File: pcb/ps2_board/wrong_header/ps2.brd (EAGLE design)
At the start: 56 x 65 mm, 35 parts, among them IC3 STM32F042F4, SW4 324_SW, U1 MAX3232

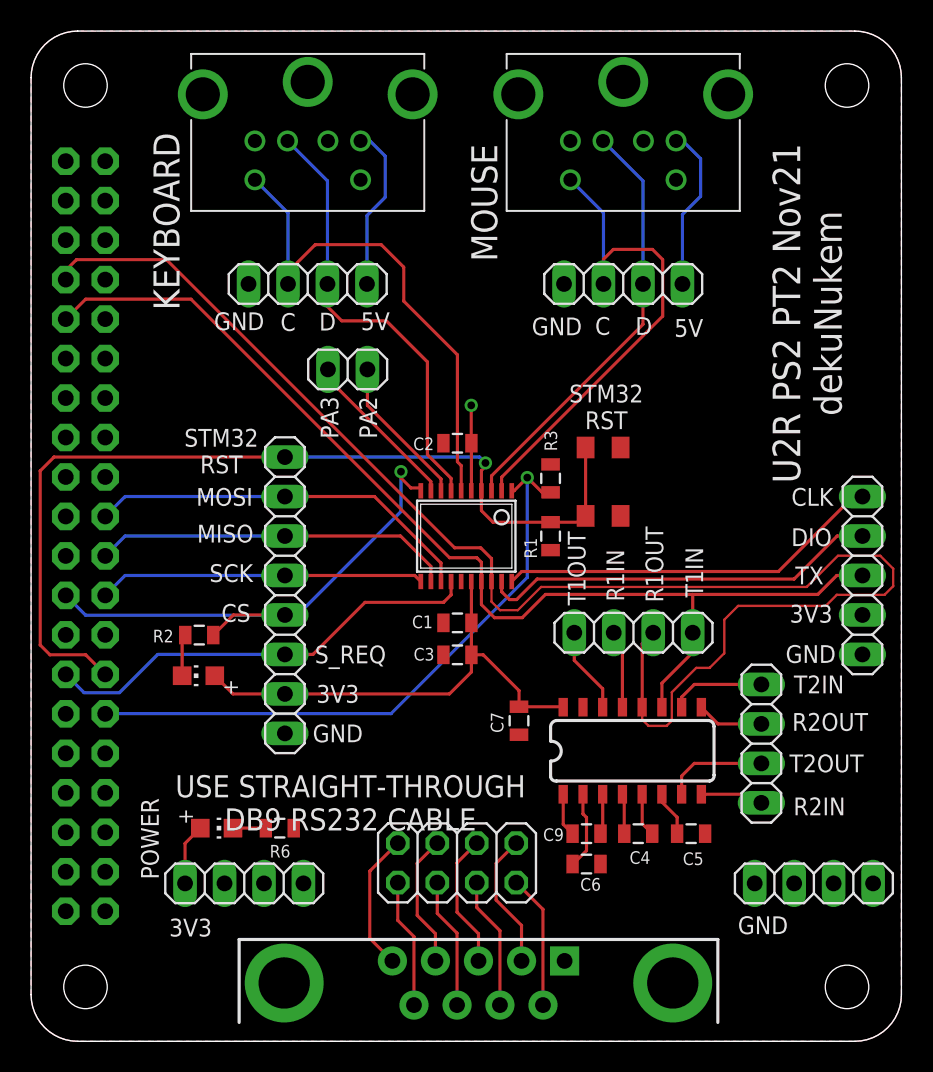
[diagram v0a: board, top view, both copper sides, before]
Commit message: fixed header orientation on ps2 board
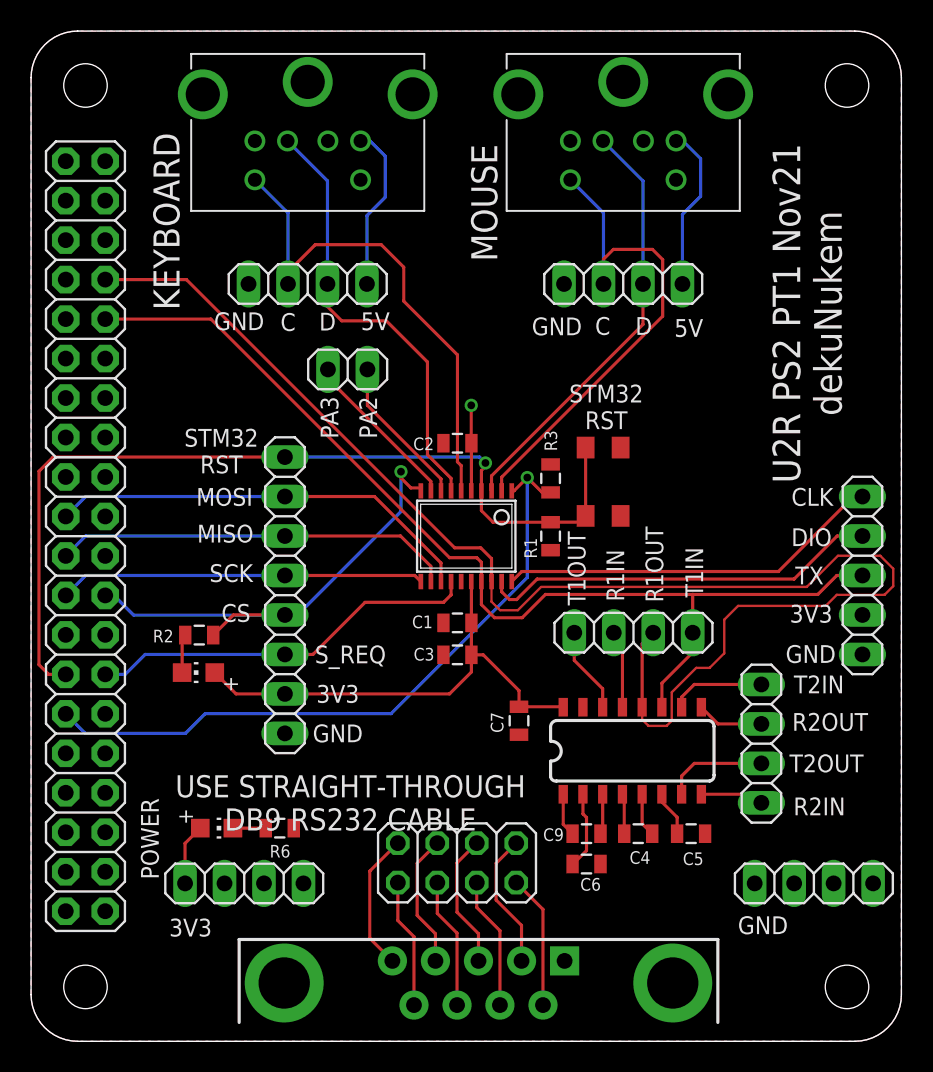
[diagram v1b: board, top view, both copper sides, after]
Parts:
- moved LED1 0.20 mm to (10.8, 23.7)
- flipped JP1 to the top
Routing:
- net STM32_RX: track 96.3 -> 92.3 mm
- net STM32_TX: track 71.1 -> 67.5 mm
- net N$9: track 40.5 -> 44.0 mm
- net SLAVE_REQ: track 28.7 -> 25.2 mm
- net SPI1_MISO: track 23.3 -> 25.8 mm
- net SPI1_SCK: track 21.0 -> 23.5 mm
- net SPI1_MOSI: track 25.1 -> 27.6 mm
- net SPI1_CS: track 34.7 -> 32.2 mm
- net N$1: track 60.3 -> 58.7 mm
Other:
- board text added: "U2R PS2 PT1 Nov21 dekuNukem"
- board text removed: "U2R PS2 PT2 Nov21 dekuNukem"

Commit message: serial mouse write working
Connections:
- net +3V3: now also R1.2
- net GND: no longer R1.2
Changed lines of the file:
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@@
 <contactref element="R6" pad="1"/>
 <contactref element="C1" pad="1"/>
-<contactref element="R1" pad="2"/>
 <contactref element="C2" pad="1"/>
 <contactref element="C3" pad="1"/>
@@
 <wire x1="9.906" y1="10.16" x2="9.906" y2="12.734" width="0.2032" layer="1"/>
 <wire x1="9.906" y1="12.734" x2="10.888" y2="13.716" width="0.2032" layer="1"/>
+<contactref element="R1" pad="2"/>
+<wire x1="28.325" y1="29.5822" x2="33.4264" y2="31.6" width="0" layer="19" extent="1-1"/>
 </signal>
 <signal name="N$1">
